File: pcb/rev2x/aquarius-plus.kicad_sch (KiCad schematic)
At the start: 216 parts, among them J1 Cassette in, J10 Audio out, J11 Hand controller 2, J12 ESP USB Host, J13 Power in, J14 FPGA spare, J15 Expansion port, J16 ESP32 spare, J2 Cassette out, J3 Amphenol GSD090012SEU, J4 Printer, J5 Hand controller 1, J6 VGA, J7 DBG, J8 USB_A, J9 USB_A, Q1 BC847C, Q2 BC847C, SW1 SW_DPDT_x2, U1 XC3S200-4TQG144, U10 IS61C5128AS-25QLI, U11 74LVC4245APW, U12 74HC166, U13 SST39SF020A-55-4C-WHE, U14 74LVC4245APW, U15 LDL1117S33R, U16 MCP1700T-2502E/TT, U17 LD1117S12, U2 SN74CBTD3861PWR, U3 MAX3221ECPWR, U4 SN74CBTD3861PWR, U5 ESP32-S2-SOLO-N4R2, U6 SN74CBTD3861PWR, U7 Z84C0010AEG, U8 SN74CBTD3861PWR, U9 74HC166, X1 ECS-5032MV-143-CN-TR, X2 ECS-5032MV-480-BN-TR

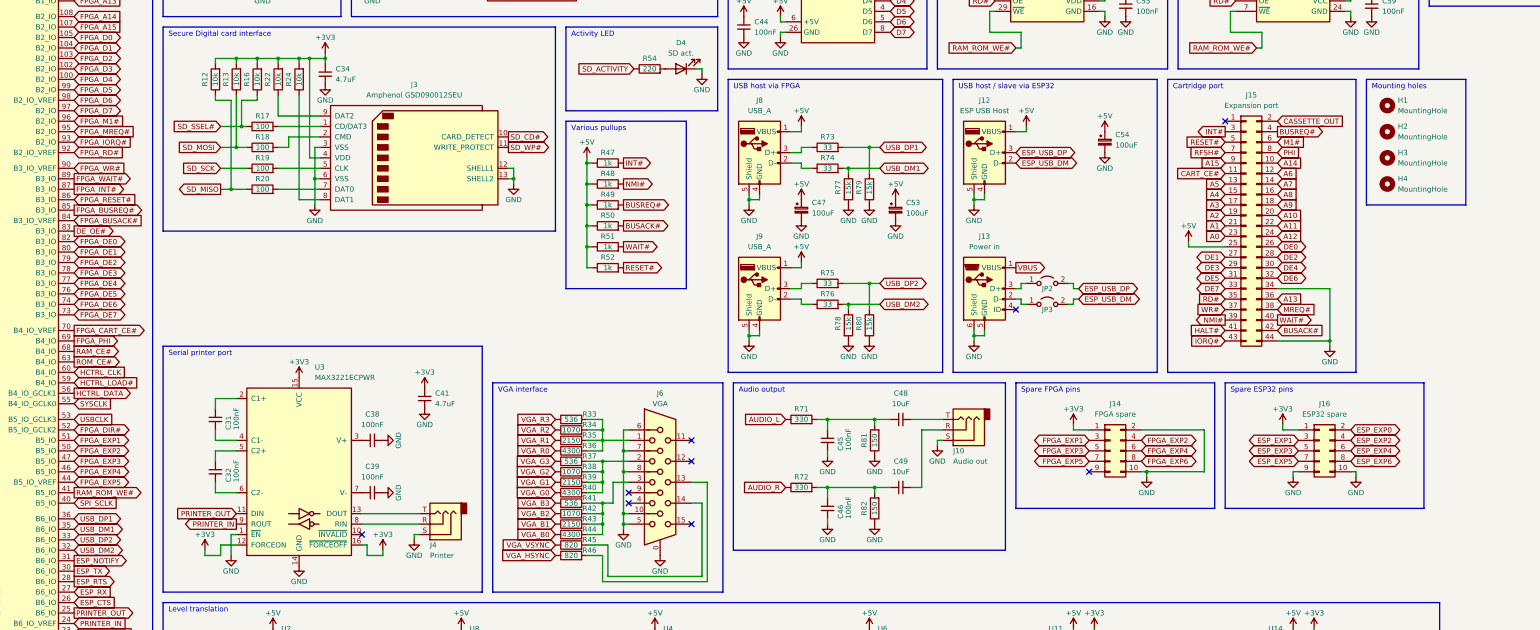
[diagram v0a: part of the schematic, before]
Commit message: Removed front USBs on PCB
- Removed front USB ports & traces
- Renamed FPGA spares
- Resized spare FPGA IO header
- Routed spares to updated header
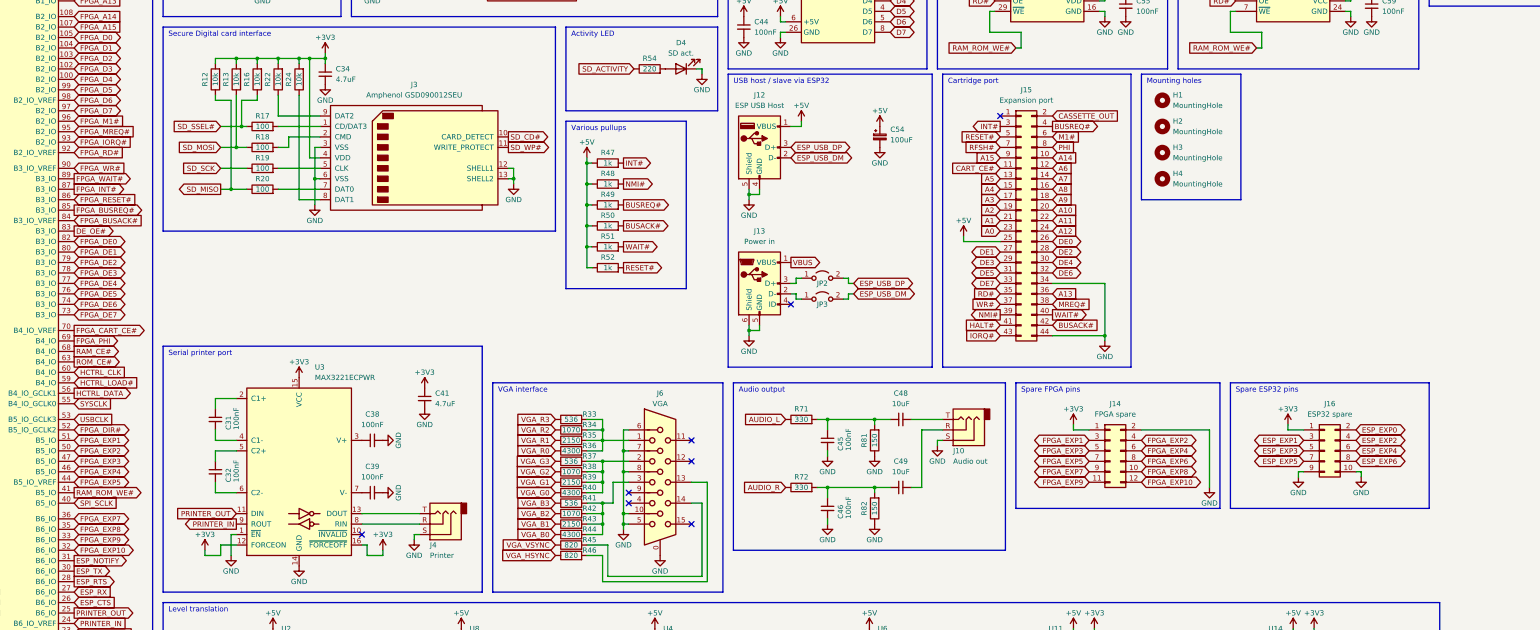
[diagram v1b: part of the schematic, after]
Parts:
- removed C47, C53: 100uF, Capacitor_SMD:CP_Elec_6.3x7.7, symbol Device:C_Polarized_Small
- removed J8, J9: USB_A, Connector_USB:USB_A_Molex_67643_Horizontal, symbol Connector:USB_A
- removed R73, R74, R75, R76: 33, Resistor_SMD:R_0603_1608Metric, symbol Device:R
- removed R77, R78, R79, R80: 15k, Resistor_SMD:R_0603_1608Metric, symbol Device:R
- J14: footprint Connector_PinHeader_2.54mm:PinHeader_2x05_P2.54mm_Vertical -> Connector_PinHeader_2.54mm:PinHeader_2x06_P2.54mm_Vertical; symbol Connector_Generic:Conn_02x05_Odd_Even -> Connector_Generic:Conn_02x06_Odd_Even
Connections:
- net USB_DP1 is gone; now on net FPGA_EXP7: U1.36 (B6_IO)
- net GND: no longer J14.10 (Pin_10)
- net FPGA_EXP7: now reaches J14.9 (Pin_9)
- net USB_DM1 renamed FPGA_EXP8
- net FPGA_EXP8: now also J14.10 (Pin_10)
- net USB_DM2 renamed FPGA_EXP10
- net FPGA_EXP10: now also J14.12 (Pin_12)
- net USB_DP2 renamed FPGA_EXP9
- net FPGA_EXP9: now also J14.11 (Pin_11)
- no-connect marks 21 -> 20
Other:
- note removed: "USB host via FPGA"
- moved on the sheet: C54, H1, H2, H3, H4, J12, J13, J15, J16, JP2, JP3

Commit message: PCB Reduction
- Remove U14
- Refactor unused FPGA pins
- Direct connect Control Pad ports to FPGA
- Direct connect DE00-07 to Z80 D0-D7
- Expand, relocate, & rewire FPGA spare IO header
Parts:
- removed C30, C51, C52, C56, C58: 100nF, Capacitor_SMD:C_0603_1608Metric, symbol Device:C_Small
- removed R63, R64, R65, R66, R67, R68, R69, R70, R91, R92, R93, R94, R95, R96, R97, R98: 4.7k, Resistor_SMD:R_0603_1608Metric, symbol Device:R
- removed U11: 74LVC4245APW, Package_SO:TSSOP-24_4.4x7.8mm_P0.65mm, symbol Logic_LevelTranslator:SN74AVC8T245PW
- removed U12, U9: 74HC166, Package_SO:SOIC-16_3.9x9.9mm_P1.27mm, symbol 74xx:74LS166
- removed X2: ECS-5032MV-480-BN-TR, Oscillator:Oscillator_SMD_SeikoEpson_SG8002LB-4Pin_5.0x3.2mm, symbol Oscillator:SG-5032CAN
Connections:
- net DE0 is gone; now on net D0: J15.26 (Pin_26)
- net DE1 is gone; now on net D1: J15.27 (Pin_27)
- net DE2 is gone; now on net D2: J15.28 (Pin_28)
- net DE3 is gone; now on net D3: J15.29 (Pin_29)
- net DE4 is gone; now on net D4: J15.30 (Pin_30)
- net DE5 is gone; now on net D5: J15.31 (Pin_31)
- net DE6 is gone; now on net D6: J15.32 (Pin_32)
- net DE7 is gone; now on net D7: J15.33 (Pin_33)
- net FPGA_DE0 is gone; now on net HC2_D04: U1.82 (B3_IO)
- net FPGA_DE1 is gone; now on net HC2_D03: U1.80 (B3_IO)
- net FPGA_DE2 is gone; now on net HC2_D05: U1.79 (B3_IO)
- net FPGA_DE3 is gone; now on net HC2_D02: U1.78 (B3_IO)
- net FPGA_DE4 is gone; now on net HC2_D06: U1.77 (B3_IO)
- net FPGA_DE5 is gone; now on net HC2_D01: U1.76 (B3_IO)
- net FPGA_DE6 is gone; now on net HC2_D07: U1.74 (B3_IO)
- net FPGA_DE7 is gone; now on net HC2_D00: U1.73 (B3_IO)
- net FPGA_DIR# is gone; now on net FPGA_EXP6: U1.52 (B5_IO_GCLK2)
- net HCTRL_CLK is gone; now on net FPGA_EXP2: U1.60 (B4_IO)
- net HCTRL_DATA is gone; now on net FPGA_EXP4: U1.56 (B4_IO_GCLK1)
- net HCTRL_LOAD# is gone; now on net FPGA_EXP3: U1.59 (B4_IO)
- net USBCLK is gone; now on net FPGA_EXP5: U1.53 (B5_IO_GCLK3)
- net +3V3: no longer U14.2 (DIR)
- net ESP_NOTIFY: no longer U1.31 (B6_IO)
- net FPGA_EXP1: now also U1.89 (B3_IO); no longer U1.51 (B5_IO)
- net FPGA_EXP2: now also J14.6 (Pin_6); no longer J14.4 (Pin_4), U1.50 (B5_IO)
- net FPGA_EXP3: no longer U1.47 (B5_IO)
- net FPGA_EXP4: now also J14.8 (Pin_8); no longer J14.6 (Pin_6), U1.46 (B5_IO)
- net FPGA_EXP5: no longer U1.44 (B5_IO_VREF)
- net FPGA_EXP6: now also J14.10 (Pin_10); no longer J14.8 (Pin_8)
- net FPGA_EXP7: now also U1.51 (B5_IO); no longer U1.36 (B6_IO)
- net FPGA_EXP8: now also J14.12 (Pin_12), U1.50 (B5_IO); no longer J14.10 (Pin_10), U1.35 (B6_IO)
- net FPGA_M1#: no longer U1.96 (B2_IO)
- net FPGA_WAIT#: no longer U1.89 (B3_IO)
- net GND: now also J14.11 (Pin_11), U14.2 (DIR)
- net HC2_D02: now reaches R86.2
- net HC2_D06: now reaches R87.2
- net HC1_D07: now reaches R61.2
- net HC1_D07: now also U1.32 (B6_IO)
- net HC1_D03: now reaches R56.2
- net HC1_D03: now also U1.46 (B5_IO)
- net HC1_D05: now reaches R57.2
- net HC1_D05: now also U1.44 (B5_IO_VREF)
- net HC1_D01: now reaches R60.2
- net HC1_D01: now also U1.33 (B6_IO)
- net HC2_D05: now reaches R85.2
- net HC1_D04: now reaches R55.2
- net HC1_D04: now also U1.47 (B5_IO)
- net HC1_D00: now reaches R62.2
- net HC1_D00: now also U1.31 (B6_IO)
- net HC1_D06: now reaches R59.2
- net HC1_D06: now also U1.35 (B6_IO)
- net HC2_D01: now reaches R88.2
- net HC2_D00: now reaches R90.2
- net HC2_D04: now reaches R83.2
- net HC2_D03: now reaches R84.2
- net HC1_D02: now reaches R58.2
- net HC1_D02: now also U1.36 (B6_IO)
- net HC2_D07: now reaches R89.2
- removed net FPGA_EXP10: J14.12 (Pin_12), U1.32 (B6_IO)
- removed net FPGA_EXP9: J14.11 (Pin_11), U1.33 (B6_IO)
- new net FPGA_EXP0: J14.4 (Pin_4), U1.96 (B2_IO)
- no-connect marks 20 -> 19
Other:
- note removed: "USB clock (48MHz)"
- moved on the sheet: C57, C60, C61, C62, C63, C64, C65, C66, C67, J11, J14, J16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

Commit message: PCB rev2x Corrections
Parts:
- J16: footprint Connector_PinHeader_2.54mm:PinHeader_2x05_P2.54mm_Vertical -> Connector_PinHeader_2.54mm:PinHeader_2x06_P2.54mm_Vertical; symbol Connector_Generic:Conn_02x05_Odd_Even -> Connector_Generic:Conn_02x06_Odd_Even
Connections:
- net DE_OE# is gone; now on net FPGA_EXP2: U1.83 (B3_IO)
- net ESP_EXP7: now also J16.9 (Pin_9)
- net FPGA_EXP2: no longer U1.60 (B4_IO)
- net FPGA_EXP3: now also U1.60 (B4_IO); no longer U1.59 (B4_IO)
- net FPGA_EXP4: now also U1.59 (B4_IO); no longer U1.56 (B4_IO_GCLK1)
- net FPGA_EXP5: now also U1.56 (B4_IO_GCLK1); no longer U1.53 (B5_IO_GCLK3)
- net FPGA_EXP6: now also U1.53 (B5_IO_GCLK3); no longer U1.52 (B5_IO_GCLK2)
- net FPGA_EXP7: now also U1.52 (B5_IO_GCLK2); no longer U1.51 (B5_IO)
- net FPGA_EXP8: now also U1.51 (B5_IO); no longer U1.50 (B5_IO)
- net GND: now also J16.12 (Pin_12); no longer J14.11 (Pin_11), J16.10 (Pin_10), J16.9 (Pin_9)
- net M1#: no longer U6.22 (B1)
- net WAIT#: no longer U6.17 (B6)
- net ESP_EXP9: now reaches U5.28 (IO35)
- net ESP_EXP9: now also J16.11 (Pin_11)
- net ESP_EXP8: now reaches U5.29 (IO36)
- net ESP_EXP8: now also J16.10 (Pin_10)
- net FPGA_M1#: no longer names the net of U6.2 (A1)
- net FPGA_WAIT#: no longer names the net of U6.7 (A6)
- new net FPGA_EXP9: J14.11 (Pin_11), U1.50 (B5_IO)

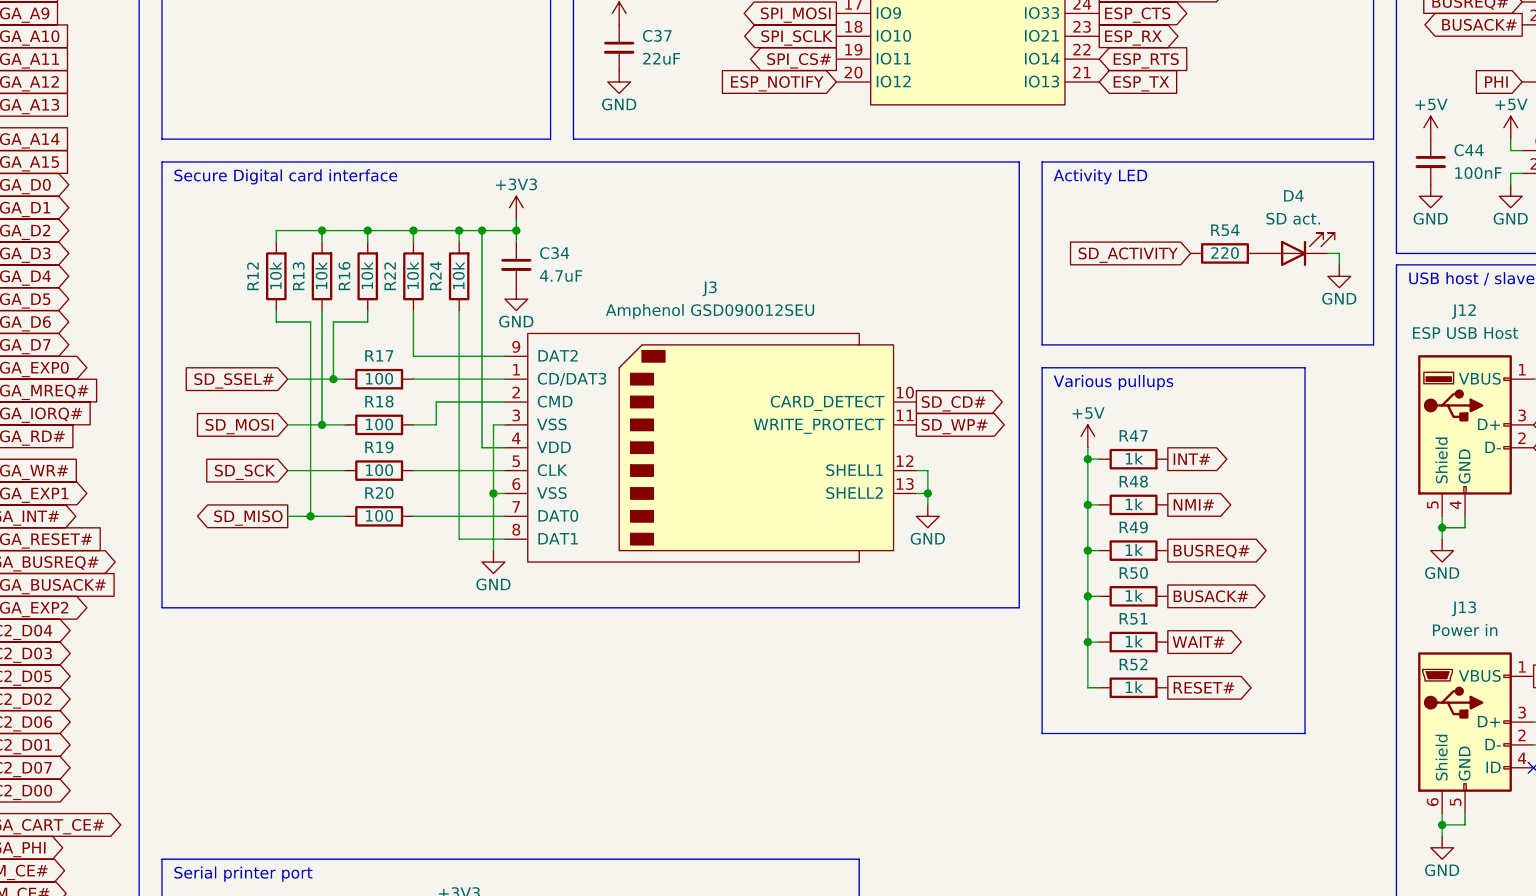
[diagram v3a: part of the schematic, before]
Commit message: Added 2n7002 as an inverter for SD card WP
Also added index dots for rotatable chips.
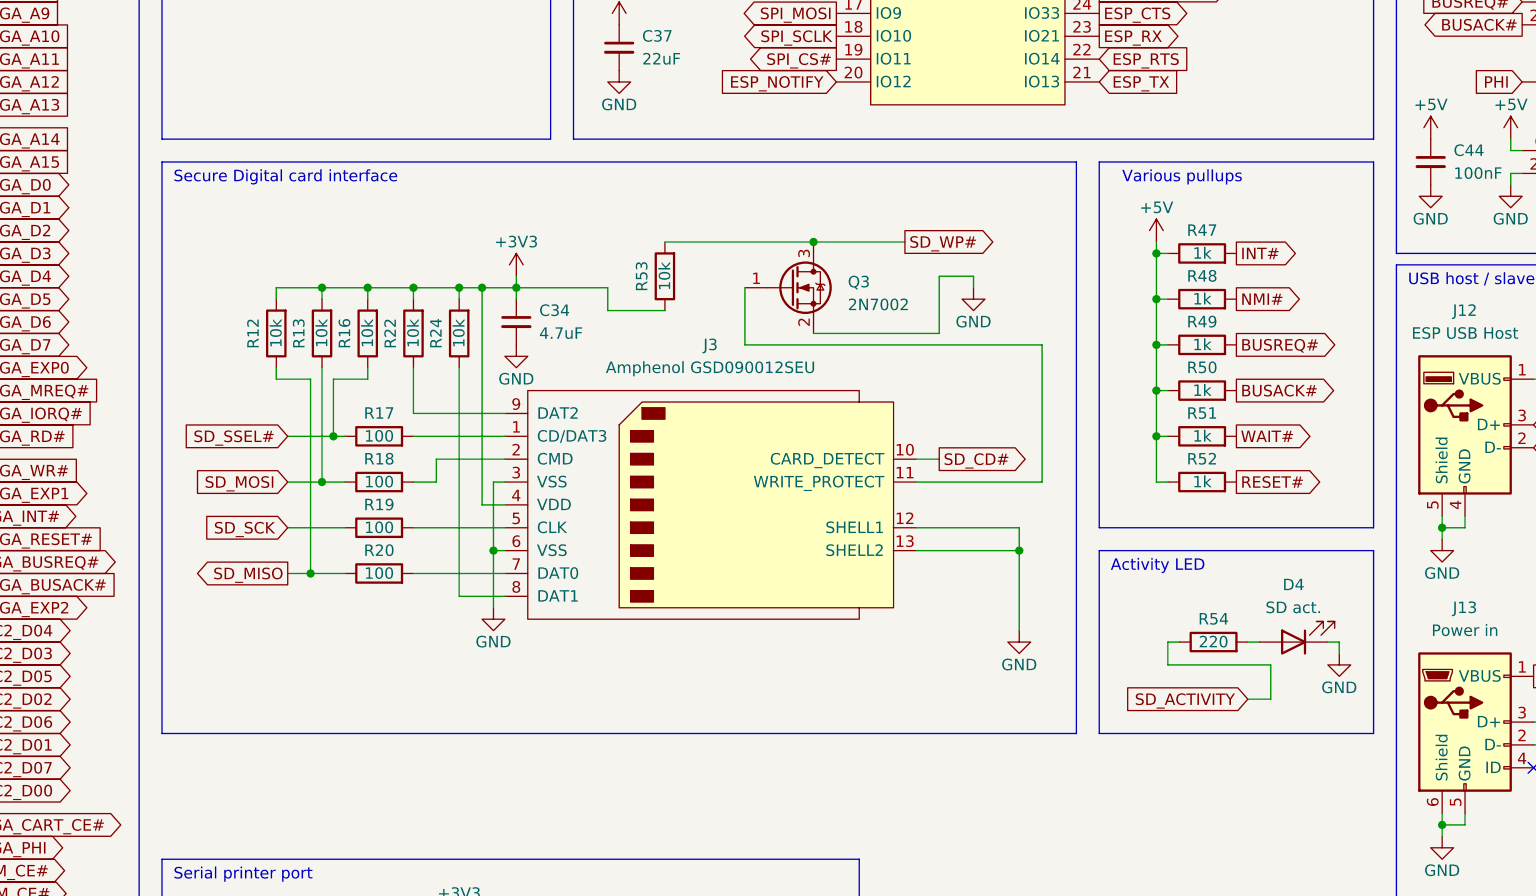
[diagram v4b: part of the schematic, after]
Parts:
- added Q3: 2N7002, Package_TO_SOT_SMD:SOT-23, symbol Transistor_FET:2N7002
- added R53: 10k, Resistor_SMD:R_0603_1608Metric, symbol Device:R
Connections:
- net +3V3: now also R53.1
- net GND: now also Q3.2 (S)
- net SD_WP#: now also Q3.3 (D), R53.2; no longer J3.11 (WRITE_PROTECT)
- new net: J3.11 (WRITE_PROTECT), Q3.1 (G)
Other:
- moved on the sheet: C34, D4, J3, R12, R13, R16, R17, R18, R19, R20, R22, R24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

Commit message: Fixes and re-indexing of components
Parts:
- renumbered C48 to C1, C63 to C10, C66 to C11, C40 to C12, C50 to C13, C32 to C14, C39 to C15, C28 to C16, C16 to C18, C20 to C19, C45 to C2, C24 to C20, C25 to C21, C11 to C22, C12 to C23, C26 to C24, C19 to C25, C42 to C26, C41 to C27, C31 to C28, C38 to C29, C49 to C3, C3 to C30, C14 to C31, C55 to C32, C43 to C33, C67 to C34, C64 to C35, C8 to C36, C9 to C37, C5 to C38, C15 to C39, C46 to C4, C13 to C40, C4 to C41, C18 to C42, C2 to C43, C1 to C44, C21 to C45, C23 to C46, C10 to C47, C6 to C48, C7 to C49, C54 to C5, C22 to C50, C27 to C51, C57 to C52, C60 to C53, C65 to C54, C62 to C55, C59 to C56, C29 to C57, C36 to C58, C37 to C59, C61 to C6, C34 to C60, C35 to C7, C44 to C8, C33 to C9, D4 to D3, J13 to J1, J15 to J10, J14 to J11, J3 to J12, J5 to J13, J11 to J14, J6 to J2, J10 to J3, J12 to J4, J2 to J5, J1 to J6, J4 to J7, J7 to J8, J16 to J9, JP3 to JP1, JP1 to JP3, R51 to R1, R33 to R10, R34 to R11, R35 to R12, R36 to R13, R37 to R14, R38 to R15, R39 to R16, R40 to R17, R41 to R18, R42 to R19, R50 to R2, R43 to R20, R44 to R21, R45 to R22, R46 to R23, R23 to R24, R71 to R25, R72 to R26, R15 to R27, R14 to R28, R25 to R29, R49 to R3, R26 to R30, R28 to R31, R31 to R32, R32 to R33, R100 to R34, R30 to R35, R29 to R36, R5 to R37, R4 to R38, R8 to R39, R48 to R4, R10 to R40, R1 to R41, R11 to R42, R2 to R43, R102 to R44, R101 to R45, R3 to R46, R6 to R47, R7 to R48, R9 to R49, R52 to R5, R99 to R50, R27 to R51, R53 to R52, R24 to R53, R20 to R54, R12 to R55, R19 to R56, R13 to R57, R18 to R58, R17 to R59, R47 to R6, R16 to R60, R22 to R61, R61 to R63, R60 to R64, R59 to R65, R58 to R66, R57 to R67, R56 to R68, R55 to R69, R81 to R7, R90 to R70, R89 to R71, R88 to R72, R87 to R73, R86 to R74, R85 to R75, R84 to R76, R83 to R77, R54 to R78, R82 to R8, R21 to R9, U7 to U1, U6 to U10, U15 to U11, U10 to U12, U5 to U13, U16 to U3, U8 to U4, U3 to U5, U4 to U6, U13 to U7, U17 to U8, U1 to U9
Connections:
- net SD_WP#: no longer R52.2
- net at J12.11 (WRITE_PROTECT), Q3.1 (G): now also R52.2
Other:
- moved on the sheet: Q3, R52
